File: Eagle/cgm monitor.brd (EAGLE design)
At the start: 116.5 x 35.5 mm, 9 parts, among them J1 PINHD-1X5, J2 PINHD-1X5

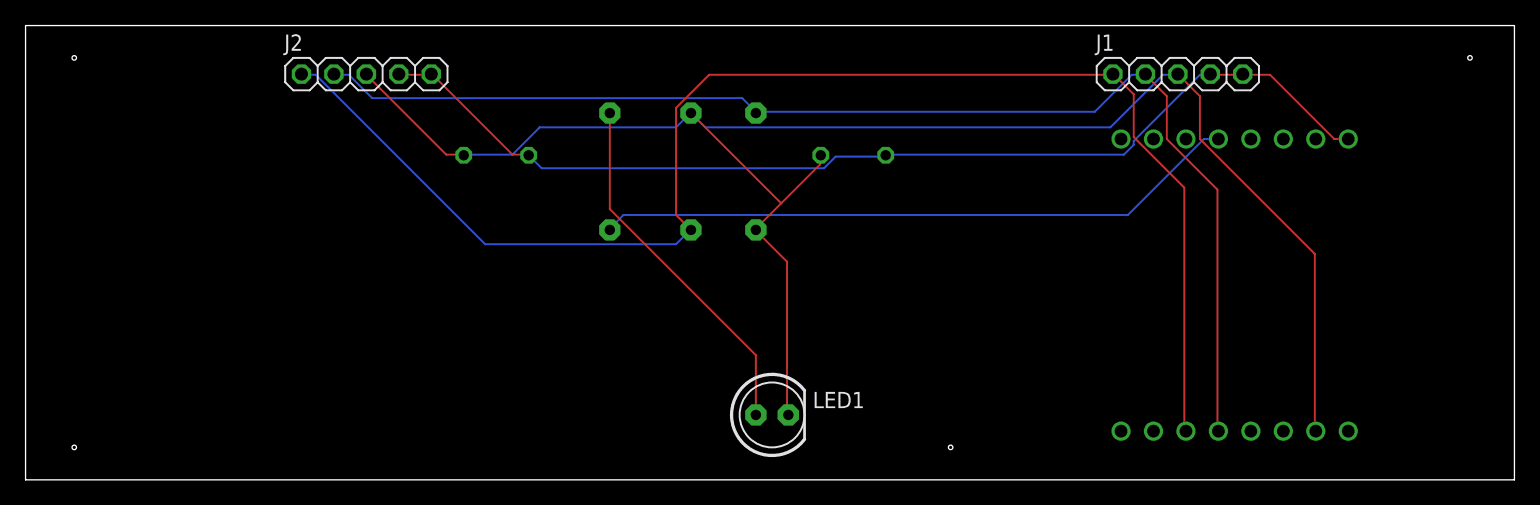
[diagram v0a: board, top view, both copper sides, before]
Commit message: Added a USB notch and flipped D1 to my standard orientation
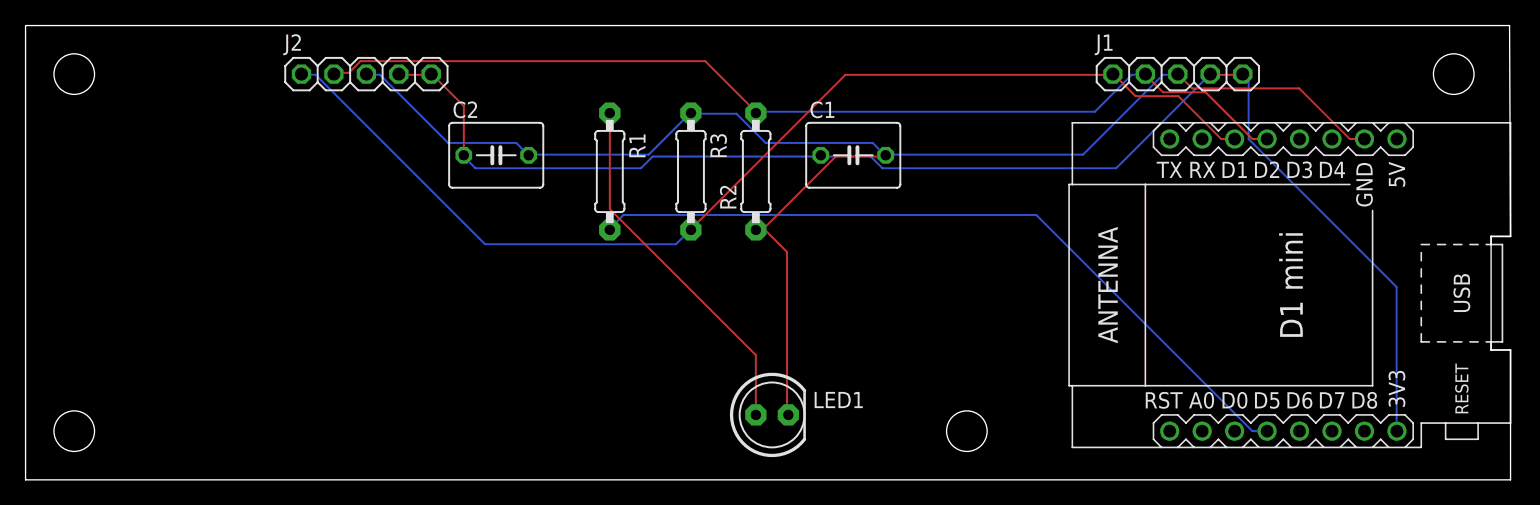
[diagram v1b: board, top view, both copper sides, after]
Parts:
- moved W1 3.81 mm to (99.1, 15.2), flipped to the top, turned to 90 degrees
- flipped C1 to the top
- flipped C2 to the top
- flipped R1 to the top
- flipped R2 to the top
- flipped R3 to the top
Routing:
- net SCL: track 112.2 -> 86.2 mm
- net 3V3: track 82.8 -> 108.4 mm
- net GND: track 135.7 -> 116.8 mm
- net SDA: track 96.4 -> 78.7 mm
- net N$3: track 50.6 -> 59.0 mm
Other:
- board size 116.5 x 35.5 mm -> 116.2 x 35.5 mm
- board text added: "CGM Monitor 5/22/2023"
- board text removed: "CGM Monitor 10/3/2019"
